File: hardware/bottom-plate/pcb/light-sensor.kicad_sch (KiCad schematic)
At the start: 4 parts

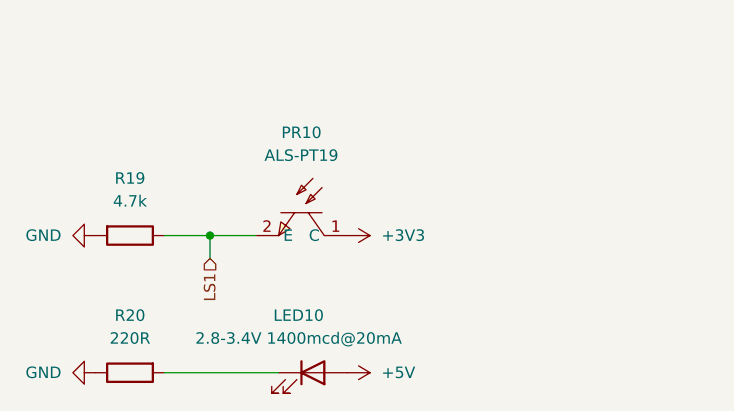
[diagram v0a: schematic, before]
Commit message: cleaned up bottom plate schematic numbering
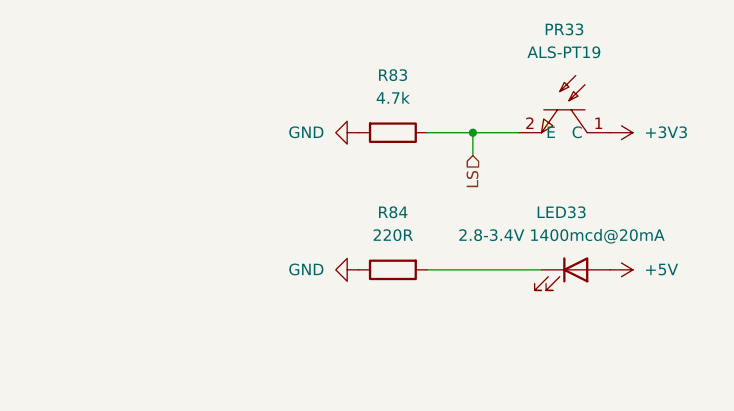
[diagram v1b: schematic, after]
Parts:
- removed LED10: 2.8-3.4V 1400mcd@20mA, Diode_SMD:D_0805_2012Metric_Pad1.15x1.40mm_HandSolder, symbol Device:LED
- removed PR10: ALS-PT19, EasyEDA:SENSORS-SMD_ALS-PT19, symbol EasyEDA:ALS-PT19-315C_L177_TR8
- removed R19: 4.7k, PCM_Resistor_SMD_AKL:R_0805_2012Metric_Pad1.15x1.40mm_HandSolder, symbol Device:R
- removed R20: 220R, PCM_Resistor_SMD_AKL:R_0805_2012Metric_Pad1.15x1.40mm_HandSolder, symbol Device:R
- added LED33: 2.8-3.4V 1400mcd@20mA, Diode_SMD:D_0805_2012Metric_Pad1.15x1.40mm_HandSolder, symbol Device:LED
- added PR33: ALS-PT19, EasyEDA:SENSORS-SMD_ALS-PT19, symbol EasyEDA:ALS-PT19-315C_L177_TR8
- added R83: 4.7k, PCM_Resistor_SMD_AKL:R_0805_2012Metric_Pad1.15x1.40mm_HandSolder, symbol Device:R
- added R84: 220R, PCM_Resistor_SMD_AKL:R_0805_2012Metric_Pad1.15x1.40mm_HandSolder, symbol Device:R
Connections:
- net +3V3: now also PR33.1 (C)
- net +5V: now also LED33.2 (A)
- net GND: now also R83.2, R84.1
- new net: LED33.1 (K), R84.2
- new net LS: PR33.2 (E), R83.1

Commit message: fixed non convention following of kicker pcb
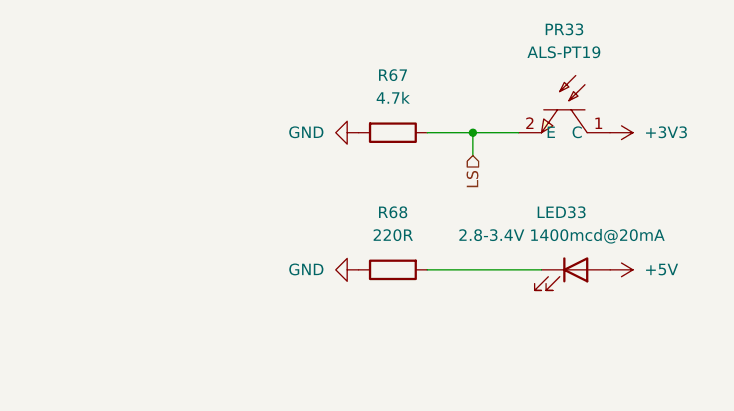
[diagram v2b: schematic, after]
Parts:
- renumbered R83 to R67, R84 to R68

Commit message: some misc bottom plate changes
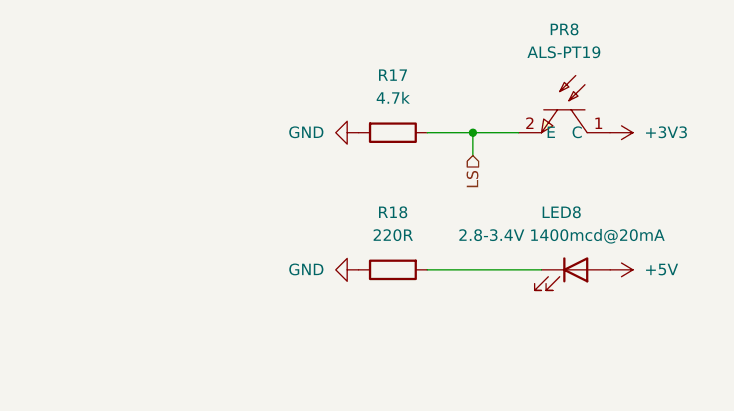
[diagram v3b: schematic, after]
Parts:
- renumbered LED33 to LED8, PR33 to PR8, R67 to R17, R68 to R18
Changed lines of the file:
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@@
 		(dnp no)
 		(fields_autoplaced yes)
-		(property "Reference" "R67"
+		(property "Reference" "R17"
 			(at 160.02 50.8 90)
 			(effects
@@
 		(dnp no)
 		(fields_autoplaced yes)
-		(property "Reference" "PR33"
+		(property "Reference" "PR8"
 			(at 179.07 45.72 90)
 			(effects
@@
 		(dnp no)
 		(fields_autoplaced yes)
-		(property "Reference" "#PWR0216"
+		(property "Reference" "#PWR0112"
 			(at 180.34 72.39 0)
 			(effects
@@
 		(dnp no)
 		(fields_autoplaced yes)
-		(property "Reference" "#PWR0215"
+		(property "Reference" "#PWR0111"
 			(at 180.34 57.15 0)
 			(effects
@@
 		(dnp no)
 		(fields_autoplaced yes)
-		(property "Reference" "LED33"
+		(property "Reference" "LED8"
 			(at 178.7525 66.04 0)
 			(effects
@@
 			)
 		)
-		(property "Datasheet" "https://www.lcsc.com/datasheet/lcsc_datasheet_2009091205_HONGLITRONIC-Hongli-Zhihui--HONGLITRONIC-HL-PSC-2012H233W-6000-7000K_C219231.pdf"
+		(property "Datasheet" "~"
 			(at 180.34 72.39 0)
 			(effects
@@
 		(dnp no)
 		(fields_autoplaced yes)
-		(property "Reference" "#PWR0214"
+		(property "Reference" "#PWR0110"
 			(at 149.86 72.39 0)
 			(effects
@@
 		(dnp no)
 		(fields_autoplaced yes)
-		(property "Reference" "#PWR0213"
+		(property "Reference" "#PWR0109"
 			(at 149.86 57.15 0)
 			(effects
@@
 		(dnp no)
 		(fields_autoplaced yes)
-		(property "Reference" "R68"
+		(property "Reference" "R18"
 			(at 160.02 66.04 90)
 			(effects

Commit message: fixed motor driver footprint (one header had markings on bottom surface for some reason), generated production files
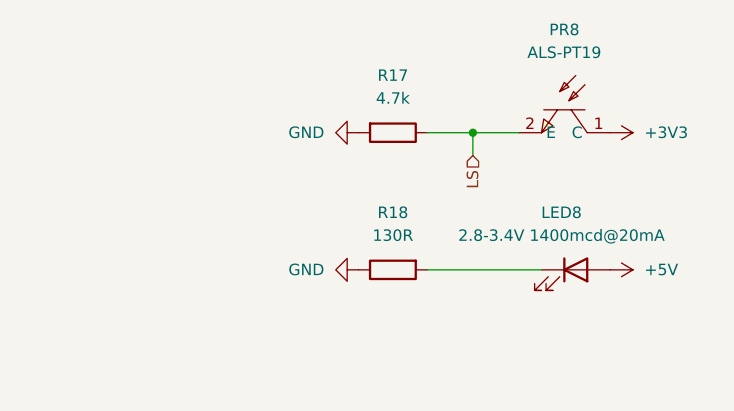
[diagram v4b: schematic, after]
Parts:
- R18: value 220R -> 130R
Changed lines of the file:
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@@
 			)
 		)
-		(property "Value" "220R"
+		(property "Value" "130R"
 			(at 160.02 68.58 90)
 			(effects

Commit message: added capacitors for motor drivers
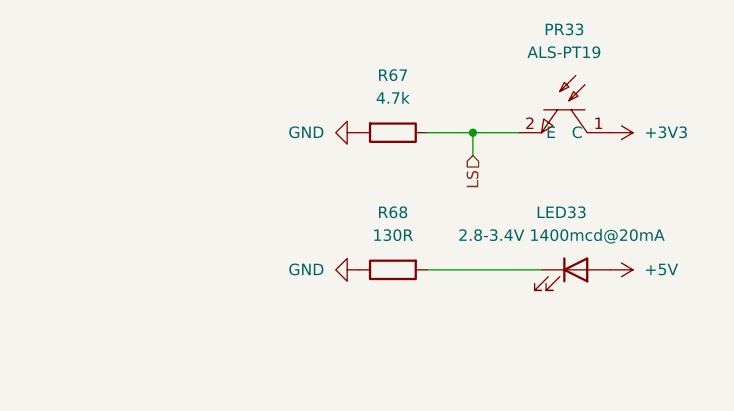
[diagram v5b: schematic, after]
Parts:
- renumbered LED8 to LED33, PR8 to PR33, R17 to R67, R18 to R68
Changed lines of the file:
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@@
 		(dnp no)
 		(fields_autoplaced yes)
-		(property "Reference" "R17"
+		(property "Reference" "R67"
 			(at 160.02 50.8 90)
 			(effects
@@
 		(dnp no)
 		(fields_autoplaced yes)
-		(property "Reference" "PR8"
+		(property "Reference" "PR33"
 			(at 179.07 45.72 90)
 			(effects
@@
 		(dnp no)
 		(fields_autoplaced yes)
-		(property "Reference" "#PWR0112"
+		(property "Reference" "#PWR0216"
 			(at 180.34 72.39 0)
 			(effects
@@
 		(dnp no)
 		(fields_autoplaced yes)
-		(property "Reference" "#PWR0111"
+		(property "Reference" "#PWR0215"
 			(at 180.34 57.15 0)
 			(effects
@@
 		(dnp no)
 		(fields_autoplaced yes)
-		(property "Reference" "LED8"
+		(property "Reference" "LED33"
 			(at 178.7525 66.04 0)
 			(effects
@@
 		(dnp no)
 		(fields_autoplaced yes)
-		(property "Reference" "#PWR0110"
+		(property "Reference" "#PWR0214"
 			(at 149.86 72.39 0)
 			(effects
@@
 		(dnp no)
 		(fields_autoplaced yes)
-		(property "Reference" "#PWR0109"
+		(property "Reference" "#PWR0213"
 			(at 149.86 57.15 0)
 			(effects
@@
 		(dnp no)
 		(fields_autoplaced yes)
-		(property "Reference" "R18"
+		(property "Reference" "R68"
 			(at 160.02 66.04 90)
 			(effects

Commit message: removed global labels from bottom plate schematic (forgot to remove it)
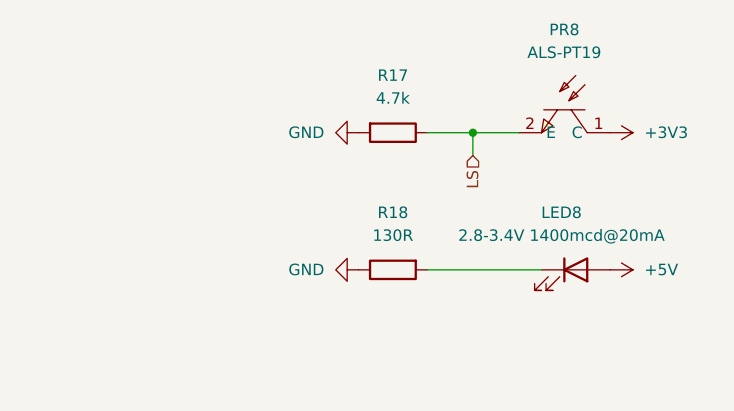
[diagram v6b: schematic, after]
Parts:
- renumbered LED33 to LED8, PR33 to PR8, R67 to R17, R68 to R18
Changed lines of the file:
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@@
 		(shape input)
 		(at 168.91 59.69 270)
-		(fields_autoplaced yes)
 		(effects
 			(font
@@
 		(dnp no)
 		(fields_autoplaced yes)
-		(property "Reference" "R67"
+		(property "Reference" "R17"
 			(at 160.02 50.8 90)
 			(effects
@@
 		(dnp no)
 		(fields_autoplaced yes)
-		(property "Reference" "PR33"
+		(property "Reference" "PR8"
 			(at 179.07 45.72 90)
 			(effects
@@
 		(dnp no)
 		(fields_autoplaced yes)
-		(property "Reference" "#PWR0216"
+		(property "Reference" "#PWR0112"
 			(at 180.34 72.39 0)
 			(effects
@@
 		(dnp no)
 		(fields_autoplaced yes)
-		(property "Reference" "#PWR0215"
+		(property "Reference" "#PWR0111"
 			(at 180.34 57.15 0)
 			(effects
@@
 		(dnp no)
 		(fields_autoplaced yes)
-		(property "Reference" "LED33"
+		(property "Reference" "LED8"
 			(at 178.7525 66.04 0)
 			(effects
@@
 		(dnp no)
 		(fields_autoplaced yes)
-		(property "Reference" "#PWR0214"
+		(property "Reference" "#PWR0110"
 			(at 149.86 72.39 0)
 			(effects
@@
 		(dnp no)
 		(fields_autoplaced yes)
-		(property "Reference" "#PWR0213"
+		(property "Reference" "#PWR0109"
 			(at 149.86 57.15 0)
 			(effects
@@
 		(dnp no)
 		(fields_autoplaced yes)
-		(property "Reference" "R68"
+		(property "Reference" "R18"
 			(at 160.02 66.04 90)
 			(effects

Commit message: bottom pcb fixed, im stupid
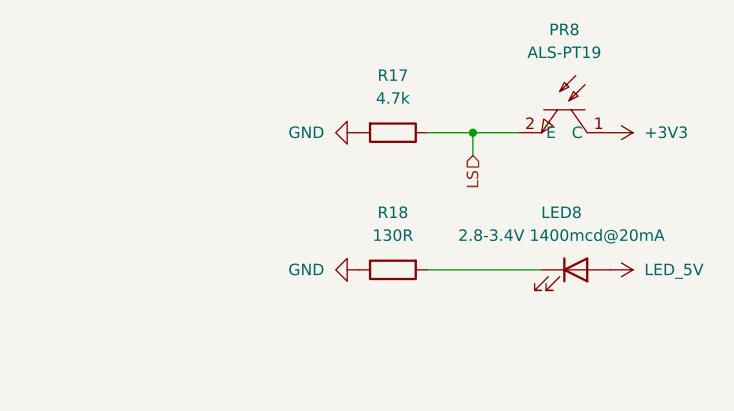
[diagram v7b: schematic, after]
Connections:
- net +5V renamed LED_5V
